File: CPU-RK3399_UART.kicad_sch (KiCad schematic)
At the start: 1 part, among them U1 RK3399

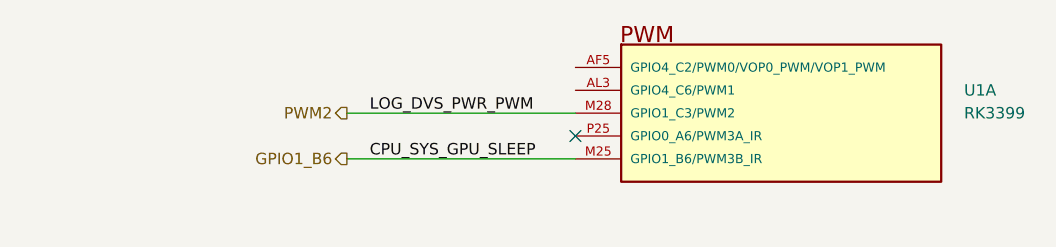
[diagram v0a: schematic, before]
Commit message: update schematic
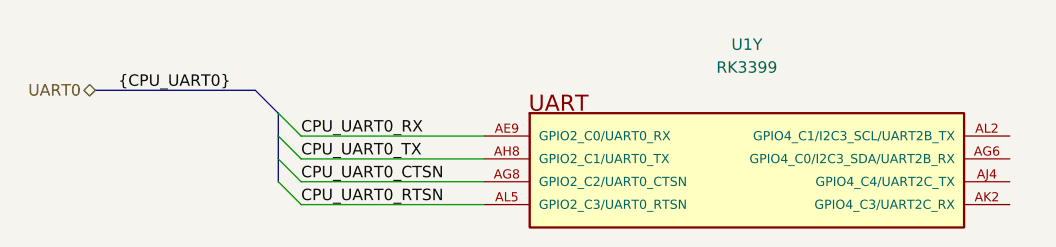
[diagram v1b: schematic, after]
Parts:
- removed U1: RK3399, footprints:BGA828C65P31X31_2100X2100X161, symbol component_library:System On Chip (SoC)/RK3399
- added U1: RK3399, footprints:BGA828C65P31X31_2100X2100X161, symbol component_library:System On Chip (SoC)/RK3399
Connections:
- new net CPU_UART0_CTSN: U1.AG8 (GPIO2_C2/UART0_CTSN)
- new net CPU_UART0_RTSN: U1.AL5 (GPIO2_C3/UART0_RTSN)
- new net CPU_UART0_RX: U1.AE9 (GPIO2_C0/UART0_RX)
- new net CPU_UART0_TX: U1.AH8 (GPIO2_C1/UART0_TX)
- no-connect marks 1 -> 0
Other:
- title: (none) -> CPU-RK3399 UART Controller
